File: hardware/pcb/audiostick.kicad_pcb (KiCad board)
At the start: 2 copper layers, 80 x 40 mm, 66 parts, among them J1 USB_B_Micro, J2 Raspberry_Pi_2_3, J3 AudioJack3_Switch, SW1 SW_Push, U1 MCP1700-3302E_SOT23, U2 PCM5102, U3 AP2161W, U4 ATtiny202-SS, U5 24AA025UID, U6 AP2127K-3.3

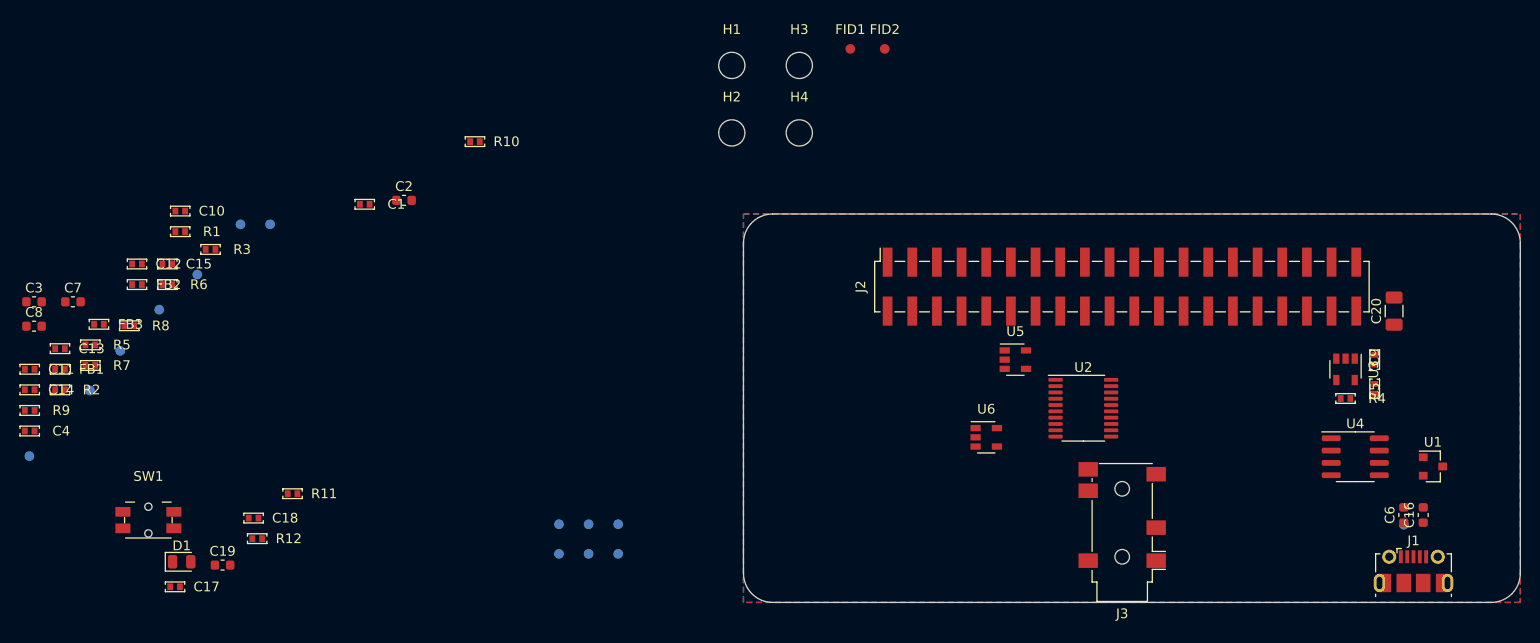
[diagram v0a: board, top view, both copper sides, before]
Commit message: More layout; BOM rationalisation
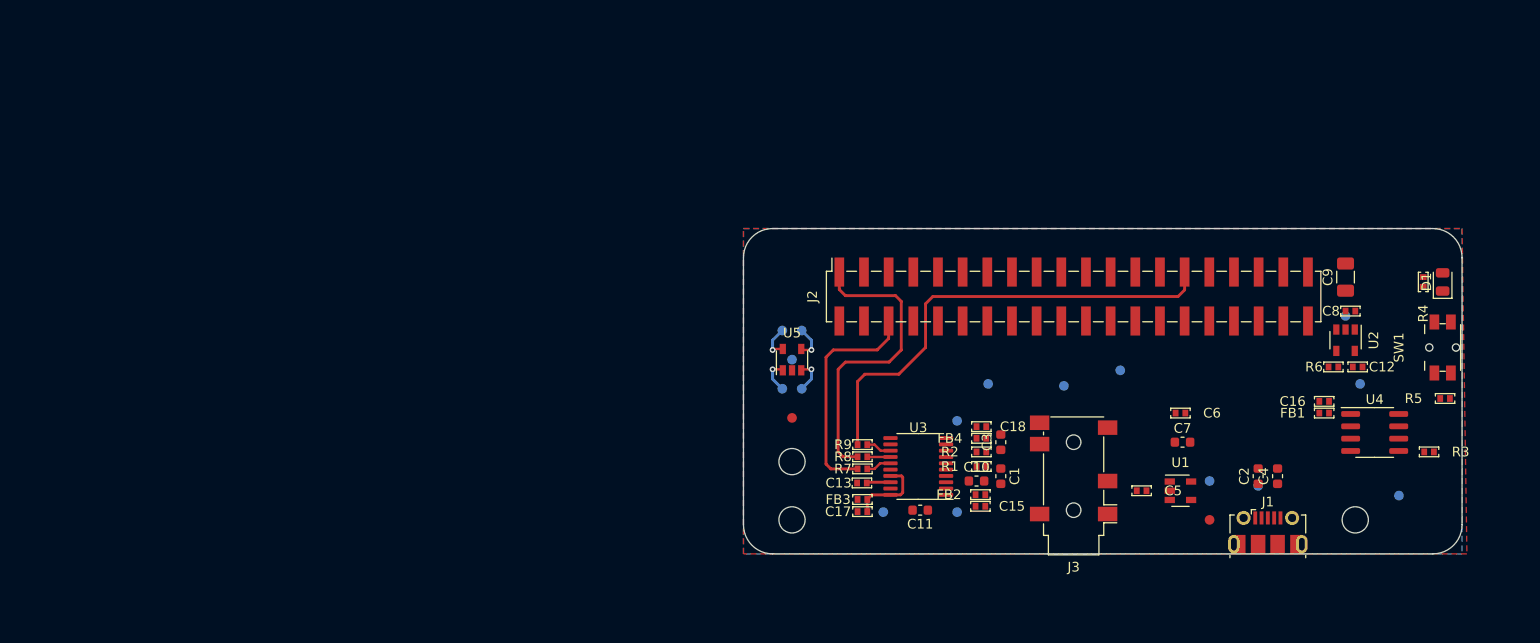
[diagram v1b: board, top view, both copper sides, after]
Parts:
- removed C14: 100n, perfect0402:perfect0402_C
- removed C19: 2u2, Capacitor_SMD:C_0603_1608Metric
- removed C20: 47u, Capacitor_SMD:C_1206_3216Metric
- removed H4: MountingHole, MountingHole:MountingHole_2.7mm_M2.5
- removed R10: 3K9, perfect0402:perfect0402_R
- removed R11: 330R, perfect0402:perfect0402_R
- removed R12: 47K, perfect0402:perfect0402_R
- removed U6: AP2127K-3.3, Package_TO_SOT_SMD:SOT-23-5
- added FB4: Ferrite_Bead_Small, perfect0402:perfect0402_R, F.Cu at (154.5, 83.1)
- added TP15: 3V3, TestPoint:TestPoint_Pad_D1.0mm, B.Cu at (193.5, 77.5)
- added TP16: UPDI, TestPoint:TestPoint_Pad_D1.0mm, B.Cu at (197.5, 89.0)
- C1: value 100n -> 2n2; footprint perfect0402:perfect0402_C -> Capacitor_SMD:C_0603_1608Metric
- C10, C11, C4: value 100n -> 2u2; footprint perfect0402:perfect0402_C -> Capacitor_SMD:C_0603_1608Metric
- C16, C6, C8: value 2u2 -> 100n; footprint Capacitor_SMD:C_0603_1608Metric -> perfect0402:perfect0402_C
- C2: value 2n2 -> 2u2
- C9: value 100n -> 47u; footprint perfect0402:perfect0402_C -> Capacitor_SMD:C_1206_3216Metric
- J2: value Raspberry_Pi_2_3 -> Conn_02x20_Odd_Even
- R1: value 47K -> 470
- R3: value 470 -> 47K
- R4: value 47K -> 330R
- R5, R6: value 0R -> 47K
- R8: value 47K -> 0R
- R9: value 3K9 -> 0R
- TP10: value GND -> AVDD
- TP11, TP12, TP13: value GND -> WP
- TP14: value 3V3 -> WP
- TP2: value 3V3 -> 3V3A
- TP5: value DVDD -> GND
- TP6: value AVDD -> GND
- TP7: value WP -> GND
- TP8: value UPDI -> GND
- TP9: value 3V3A -> DVDD
- U1: value MCP1700-3302E_SOT23 -> AP2127K-3.3; footprint Package_TO_SOT_SMD:SOT-23 -> Package_TO_SOT_SMD:SOT-23-5
- U2: value PCM5102 -> AP2161W; footprint Package_SO:TSSOP-20_4.4x6.5mm_P0.65mm -> Package_TO_SOT_SMD:SOT-23-5
- U3: value AP2161W -> PCM5102; footprint Package_TO_SOT_SMD:SOT-23-5 -> Package_SO:TSSOP-20_4.4x6.5mm_P0.65mm
- moved R5 139.6 mm to (202.2, 79.0), turned to 180 degrees
- moved C8 135.6 mm to (192.5, 70.0), turned to 180 degrees
- moved SW1 134.5 mm to (202.0, 73.8), turned to 90 degrees
- moved D1 133.0 mm to (202.0, 67.0), turned to 90 degrees
- moved FB1 130.3 mm to (189.8, 80.5), turned to 180 degrees
- moved TP4 129.5 mm to (192.0, 70.5)
- moved C4 128.6 mm to (185.0, 87.0), turned to 90 degrees
- moved R3 127.2 mm to (200.6, 84.5)
- moved C12 126.1 mm to (193.2, 75.8)
- moved TP2 121.6 mm to (178.0, 87.5)
- moved R6 120.4 mm to (190.8, 75.8)
- moved C7 115.2 mm to (175.2, 83.5)
- moved C3 100.6 mm to (156.5, 83.5), turned to 90 degrees
- moved TP6 97.2 mm to (163.0, 77.7)
- moved TP7 95.6 mm to (168.8, 76.1)
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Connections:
- C1 pad 1: VBUS -> Net-(C1-Pad1)
- C11 pad 1: +3V3 -> Net-(C11-Pad1)
- C11 pad 2: GND -> Net-(C11-Pad2)
- C12 pad 1: +3V3 -> VBUS
- C16 pad 1: VBUS -> /3V3M
- C17 pad 1: VBUS -> Net-(C17-Pad1)
- C18 pad 1: +3.3VA -> Net-(C18-Pad1)
- C2 pad 1: Net-(C2-Pad1) -> VBUS
- C4 pad 1: +3V3 -> VBUS
- C5 pad 1: +5V -> VBUS
- C6 pad 1: VBUS -> +3.3VA
- C7 pad 1: Net-(C7-Pad1) -> +3.3VA
- C8 pad 1: Net-(C8-Pad1) -> +5V
- C8 pad 2: Net-(C8-Pad2) -> GND
- C9 pad 1: VBUS -> +5V
- FB1 pad 1: +3.3VA -> /3V3M
- FB1 pad 2: Net-(C13-Pad1) -> +3.3VA
- FB2 pad 2: Net-(C14-Pad1) -> Net-(C15-Pad1)
- FB3 pad 2: Net-(C15-Pad1) -> Net-(C17-Pad1)
- J2 pad 1: (no net) -> /DIN
- J2 pad 11: /REQ -> GND
- J2 pad 12: /BCK -> (no net)
- J2 pad 13: /ACK -> (no net)
- J2 pad 14: GND -> (no net)
- J2 pad 16: (no net) -> GND
- J2 pad 2: +5V -> GND
- J2 pad 20: GND -> (no net)
- J2 pad 21: (no net) -> GND
- J2 pad 25: GND -> (no net)
- J2 pad 27: /ID_SD -> (no net)
- J2 pad 28: /ID_SC -> /ACK
- J2 pad 29: (no net) -> /BCK
- J2 pad 30: GND -> /REQ
- J2 pad 32: (no net) -> GND
- J2 pad 34: GND -> (no net)
- J2 pad 35: /LRCK -> GND
- J2 pad 37: (no net) -> +5V
- J2 pad 39: GND -> +5V
- J2 pad 4: +5V -> (no net)
- J2 pad 40: /DIN -> (no net)
- J2 pad 6: GND -> /LRCK
- J2 pad 7: (no net) -> GND
- J2 pad 9: GND -> (no net)
- R1 pad 1: GND -> Net-(C1-Pad1)
- R1 pad 2: /ACK -> /OUTL_RAW
- R2 pad 1: Net-(C2-Pad1) -> Net-(C3-Pad1)
- R2 pad 2: /OUTL_RAW -> /OUTR_RAW
- R3 pad 1: Net-(C3-Pad1) -> GND
- R3 pad 2: /OUTR_RAW -> /ACK
- R4 pad 1: /~EN -> Net-(D1-Pad2)
- R4 pad 2: VBUS -> /LED
- R5 pad 1: Net-(R5-Pad1) -> /SW
- R5 pad 2: /LRCK -> /3V3M
- R6 pad 1: Net-(R6-Pad1) -> /~EN
- R6 pad 2: /DIN -> VBUS
- R7 pad 2: /BCK -> /LRCK
- R8 pad 2: +3V3 -> /DIN
- R9 pad 1: /ID_SC -> Net-(R9-Pad1)
- R9 pad 2: +3V3 -> /BCK
- TP10 pad 1: GND -> Net-(C18-Pad1)
- TP11 pad 1: GND -> /ID_SD
- TP12 pad 1: GND -> /ID_SC
- TP13 pad 1: GND -> Net-(TP13-Pad1)
- TP2 pad 1: +3V3 -> +3.3VA
- TP3 pad 1: Net-(C13-Pad1) -> Net-(C15-Pad1)
- TP5 pad 1: Net-(C14-Pad1) -> GND
- TP6 pad 1: Net-(C15-Pad1) -> GND
- TP7 pad 1: Net-(R8-Pad1) -> GND
- TP8 pad 1: Net-(TP8-Pad1) -> GND
- TP9 pad 1: +3.3VA -> Net-(C17-Pad1)
- U1 pad 1: GND -> VBUS
- U1 pad 2: +3V3 -> GND
- U2 pad 1: Net-(C13-Pad1) -> +5V
- U2 pad 2: Net-(C8-Pad1) -> GND
- U2 pad 3: GND -> (no net)
- U2 pad 4: Net-(C8-Pad2) -> /~EN
- U2 pad 5: Net-(C7-Pad1) -> VBUS
- U3 pad 1: +5V -> Net-(C15-Pad1)
- U3 pad 2: GND -> Net-(C11-Pad1)
- U3 pad 3: (no net) -> GND
- U3 pad 4: /~EN -> Net-(C11-Pad2)
- U3 pad 5: VBUS -> Net-(C10-Pad1)
- U4 pad 1: +3V3 -> /3V3M
- U4 pad 6: Net-(TP8-Pad1) -> Net-(TP16-Pad1)
- U5 pad 5: Net-(R8-Pad1) -> Net-(TP13-Pad1)
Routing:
- net /BCK: track 0.00 -> 48.6 mm
- net /DIN: track 0.00 -> 31.7 mm
- net /LRCK: track 0.00 -> 23.5 mm
- net Net-(C17-Pad1): track 0.00 -> 8.21 mm
- net Net-(TP13-Pad1): track 0.00 -> 3.51 mm, vias 0 -> 1
- net /ID_SD: track 0.00 -> 3.51 mm, vias 0 -> 1
- net /ID_SC: track 0.00 -> 3.51 mm, vias 0 -> 1
- net +3V3: track 0.00 -> 3.51 mm, vias 0 -> 1
- net Net-(R9-Pad1): track 0.00 -> 2.65 mm
- net Net-(R7-Pad1): track 0.00 -> 2.63 mm
- net Net-(C13-Pad1): track 0.00 -> 2.47 mm
- net Net-(R8-Pad1): track 0.00 -> 2.40 mm
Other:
- board size 80 x 40 mm -> 74 x 33.5 mm

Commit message: More layout
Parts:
- moved TP7 26.0 mm to (194.0, 69.5)
- moved C8 2.24 mm to (194.5, 71.0), turned to 270 degrees
- moved C12 1.00 mm to (193.2, 74.8)
- moved R6 1.00 mm to (190.8, 74.8)
- moved TP4 1.00 mm to (192.0, 69.5)
- moved U2 1.00 mm to (192.0, 72.0)
- moved C18 0.75 mm to (153.8, 81.9)
- moved FB4 0.75 mm to (153.8, 83.1)
- moved C15 0.65 mm to (153.8, 90.1)
- moved FB2 0.65 mm to (153.8, 88.9)
- moved TP10 0.50 mm to (151.5, 81.3)
- moved TP3 0.50 mm to (151.5, 90.7)
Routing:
- net Net-(C18-Pad1): track 0.00 -> 6.98 mm, vias 0 -> 1
- net Net-(C15-Pad1): track 0.00 -> 6.37 mm, vias 0 -> 1
- net Net-(C11-Pad2): track 0.00 -> 5.74 mm
- net Net-(C11-Pad1): track 0.00 -> 3.67 mm
- net /OUTR_RAW: track 0.00 -> 3.35 mm
- net /OUTL_RAW: track 0.00 -> 3.27 mm
- net Net-(C10-Pad1): track 0.00 -> 2.86 mm
- net Net-(C17-Pad1): track 8.21 -> 11.0 mm, vias 0 -> 1
- net GND: track 0.00 -> 2.10 mm, vias 0 -> 2
- net /~EN: track 0.00 -> 1.98 mm
- net Net-(C3-Pad1): track 0.00 -> 1.59 mm
- net Net-(C1-Pad1): track 0.00 -> 1.59 mm
- net +5V: track 0.00 -> 1.50 mm, vias 0 -> 1
- added copper zone on F.Cu, net +5V

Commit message: Finish preliminary layout
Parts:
- moved TP8 40.4 mm to (195.0, 84.5)
- moved C7 20.3 mm to (156.5, 91.2), turned to 90 degrees
- moved C6 8.68 mm to (173.2, 89.0), turned to 90 degrees
- moved C5 8.27 mm to (179.2, 88.0), turned to 270 degrees
- moved TP16 6.96 mm to (195.0, 82.5)
- moved TP2 4.85 mm to (173.2, 88.5), turned to 180 degrees
- moved TP15 3.35 mm to (195.0, 80.5)
- moved R5 3.26 mm to (200.5, 81.8), turned to 0 degrees
- moved U1 1.25 mm to (176.2, 88.5), turned to 180 degrees
- moved R3 0.10 mm to (200.5, 84.5), turned to 180 degrees
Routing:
- net +3.3VA: track 0.00 -> 81.2 mm, vias 0 -> 6
- net /ACK: track 0.00 -> 40.9 mm, vias 0 -> 2
- net /REQ: track 0.00 -> 28.4 mm, vias 0 -> 2
- net /LED: track 0.00 -> 18.9 mm
- net /3V3M: track 0.00 -> 16.0 mm, vias 0 -> 2
- net /SW: track 0.00 -> 14.5 mm
- net /~EN: track 1.98 -> 13.8 mm, vias 0 -> 2
- net Net-(TP16-Pad1): track 0.00 -> 6.88 mm, vias 0 -> 1
- net GND: track 2.10 -> 6.00 mm, vias 2 -> 45
- net Net-(D1-Pad2): track 0.00 -> 2.18 mm
- net VBUS: track 0.00 -> 1.60 mm
- added copper zone on F.Cu, net VBUS
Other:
- board text added: "AudioStick awjlogan 2020"
- board text added: "BOTTOM"
- board text added: "TOP"

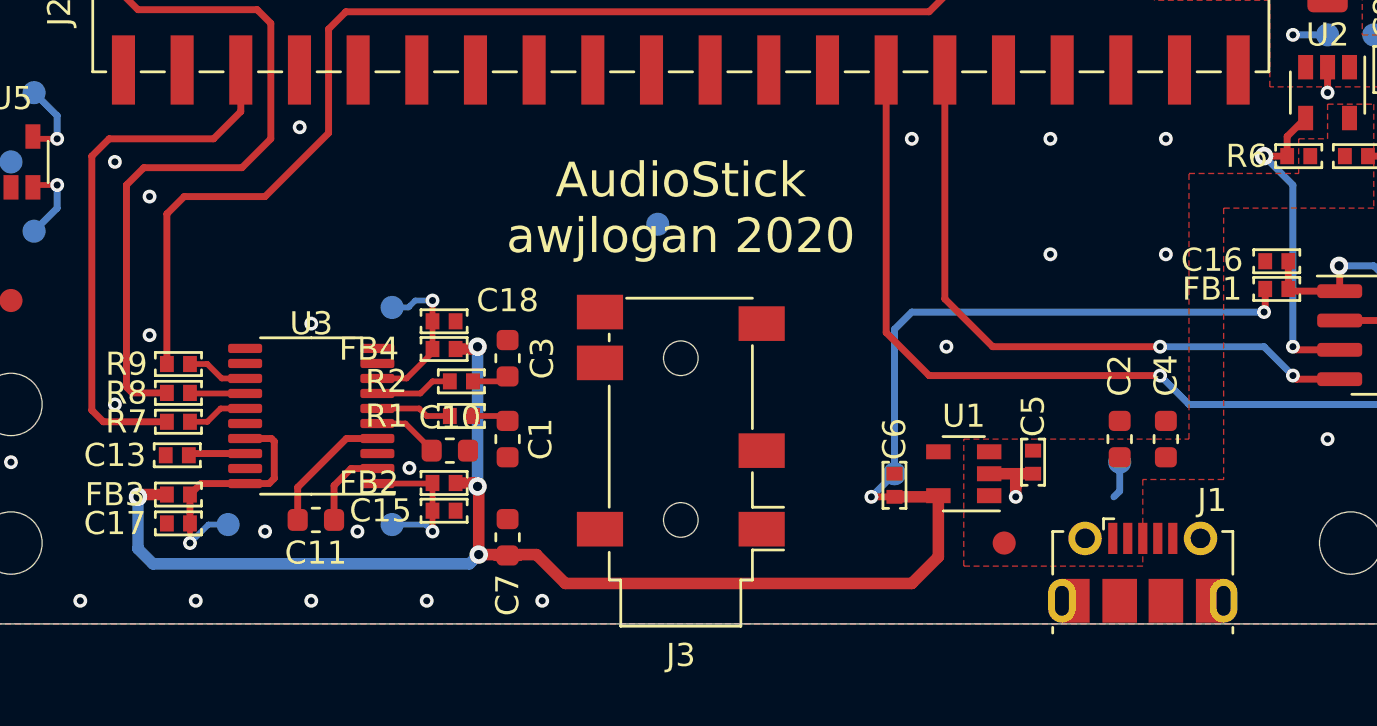
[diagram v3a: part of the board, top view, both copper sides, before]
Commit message: Change EEPROM and more layout revision
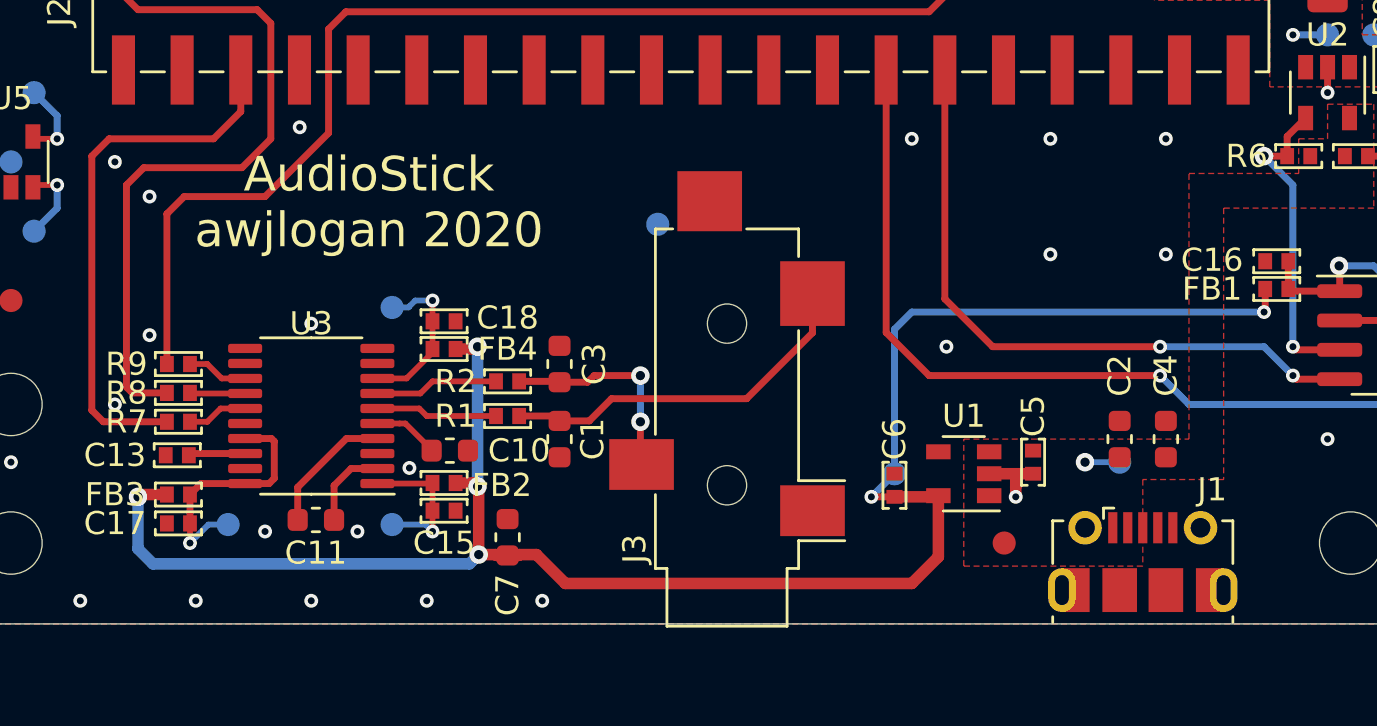
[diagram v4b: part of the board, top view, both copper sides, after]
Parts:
- J3: footprint Connector_Audio:Jack_3.5mm_PJ311_Horizontal -> Connector_Audio:Jack_3.5mm_CUI_SJ-3524-SMT_Horizontal
- U5: value 24AA025UID -> AT24CS01-STUM
- moved C3 2.26 mm to (158.8, 83.8)
- moved C1 2.25 mm to (158.8, 87.0)
- moved J3 2.02 mm to (166.0, 86.5)
- moved R1 2.00 mm to (156.5, 86.0)
- moved R2 2.00 mm to (156.5, 84.5)
- moved J1 0.46 mm to (184.0, 92.3)
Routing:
- net Net-(C1-Pad1): track 1.59 -> 16.1 mm
- net Net-(C3-Pad1): track 1.59 -> 9.26 mm, vias 0 -> 2
- net /OUTR_RAW: track 3.35 -> 5.35 mm
- net /OUTL_RAW: track 3.27 -> 5.27 mm
- net VBUS: track 1.60 -> 1.50 mm, vias 0 -> 1
